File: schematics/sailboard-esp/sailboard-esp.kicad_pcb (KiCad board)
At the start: 2 copper layers, 91.4 x 51.4 mm, 40 parts, among them IC1 TXB0108PWR, U1 AP2112K-3.3, U2 L293D

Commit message: added changelog and tweaks.
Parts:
- removed the REF** at (228.6, 49.8)
- added C4: 470uF, Capacitor_THT:CP_Radial_D8.0mm_P3.50mm, F.Cu at (227.1, 50.4)
- moved RUDDER1 4.43 mm to (238.0, 56.9), turned to 90 degrees
- moved SOLARIN1 1.60 mm to (236.3, 62.8)
- moved BATCHRG 0.93 mm to (236.3, 69.8)
- renumbered BATCHRG1 to BATCHRG
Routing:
- net +5V: track 245.8 -> 264.5 mm
- net GND: track 353.1 -> 367.1 mm
- net /RUDDER_PWM_5V: track 43.3 -> 39.7 mm
- net /Power/Solar Pos: track 26.9 -> 28.5 mm
- net /Power/Battery Charge Pos: track 28.7 -> 29.6 mm
- net /Power/Battery Charge Neg: track 7.62 -> 6.96 mm
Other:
- board text added: "SailBOARD 1.3 (12/9/22) by rmcl"
- board text removed: "SailBOARD 1.2 (12/9/22) by rmcl"

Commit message: v1.3.
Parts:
- added R6: 47K ARRAY, YC164-JR-0747KL:RESCAXE80P320X160X70-8N, F.Cu at (177.9, 66.5)
- added R7: 47K ARRAY, YC164-JR-0747KL:RESCAXE80P320X160X70-8N, F.Cu at (156.2, 65.0)
- moved ArduCam1 17.4 mm to (163.4, 25.0), turned to 0 degrees
- moved C2 1.23 mm to (171.4, 30.9)
- moved C1 0.28 mm to (209.6, 39.4)
- renumbered BATCHRG to BATCHRG1
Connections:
- COMPASS1 pad 1: GND -> +3.3V
- COMPASS1 pad 2: +3.3V -> GND
- ESP32 pad 11: unconnected-(ESP32-Pad11) -> /Microcontroller/PROP_PWM
- ESP32 pad 25: Net-(ESP32-Pad25) -> unconnected-(ESP32-Pad25)
- IC1 pad 4: Net-(ESP32-Pad25) -> /Microcontroller/PROP_PWM
- IRIDIUM1 pad 1: /IRIDIUM_RX -> GND
- IRIDIUM1 pad 10: GND -> /IRIDIUM_RX
- IRIDIUM1 pad 3: unconnected-(IRIDIUM1-Pad3) -> +5V
- IRIDIUM1 pad 4: unconnected-(IRIDIUM1-Pad4) -> /IRIDIUM_SLEEP
- IRIDIUM1 pad 5: /IRIDIUM_RING -> /IRIDIUM_TX
- IRIDIUM1 pad 6: /IRIDIUM_TX -> /IRIDIUM_RING
- IRIDIUM1 pad 7: /IRIDIUM_SLEEP -> unconnected-(IRIDIUM1-Pad7)
- IRIDIUM1 pad 8: +5V -> unconnected-(IRIDIUM1-Pad8)
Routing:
- net +3.3V: track 255.0 -> 274.8 mm, vias 2 -> 7
- net /Microcontroller/PROP_PWM: track 0.00 -> 19.5 mm
- net Net-(ESP32-Pad25): track 18.4 -> 0.00 mm
- net /ARDUCAM_CS: track 66.8 -> 84.8 mm
- net /MOSI: track 22.2 -> 39.1 mm
- net /SDCARD_SCK: track 44.1 -> 59.5 mm, vias 1 -> 3
- net GND: track 367.1 -> 378.7 mm, vias 3 -> 4
- net /SDCARD_D0: track 66.1 -> 76.5 mm, vias 1 -> 3
- net /SCL: track 113.2 -> 103.4 mm, vias 2 -> 1
- net /SDCARD_D1: track 61.7 -> 70.3 mm
- net /SCK: track 39.7 -> 47.6 mm
- net /IRIDIUM_RX: track 69.8 -> 77.3 mm
- net /IRIDIUM_SLEEP: track 48.2 -> 41.5 mm
- net /SDA: track 130.3 -> 137.0 mm
- net /SDCARD_CMD: track 61.9 -> 68.4 mm
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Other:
- board text added: "SailBOARD 1.3 (12/22/22) by rmcl"
- board text removed: "SailBOARD 1.3 (12/9/22) by rmcl"

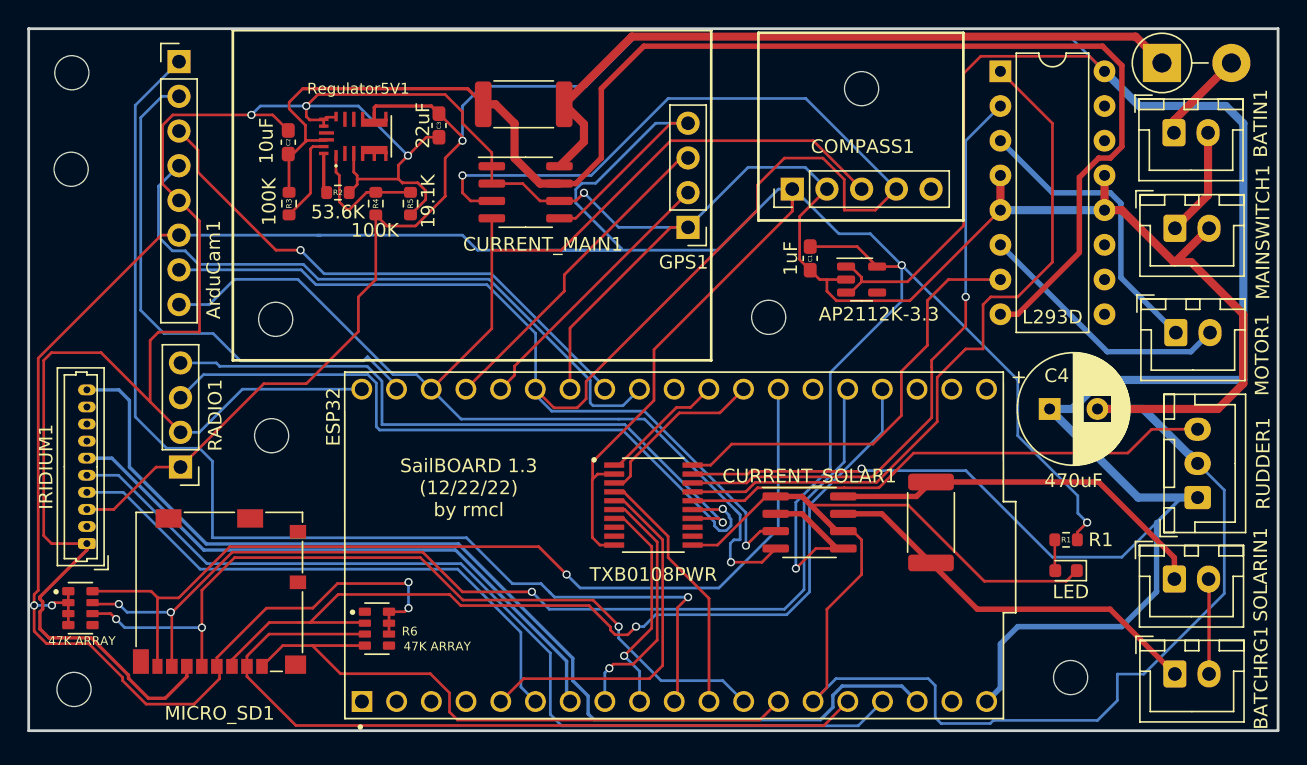
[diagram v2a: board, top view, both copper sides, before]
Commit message: rearrange pins to avoid ESP32 reserved / wonky pins.
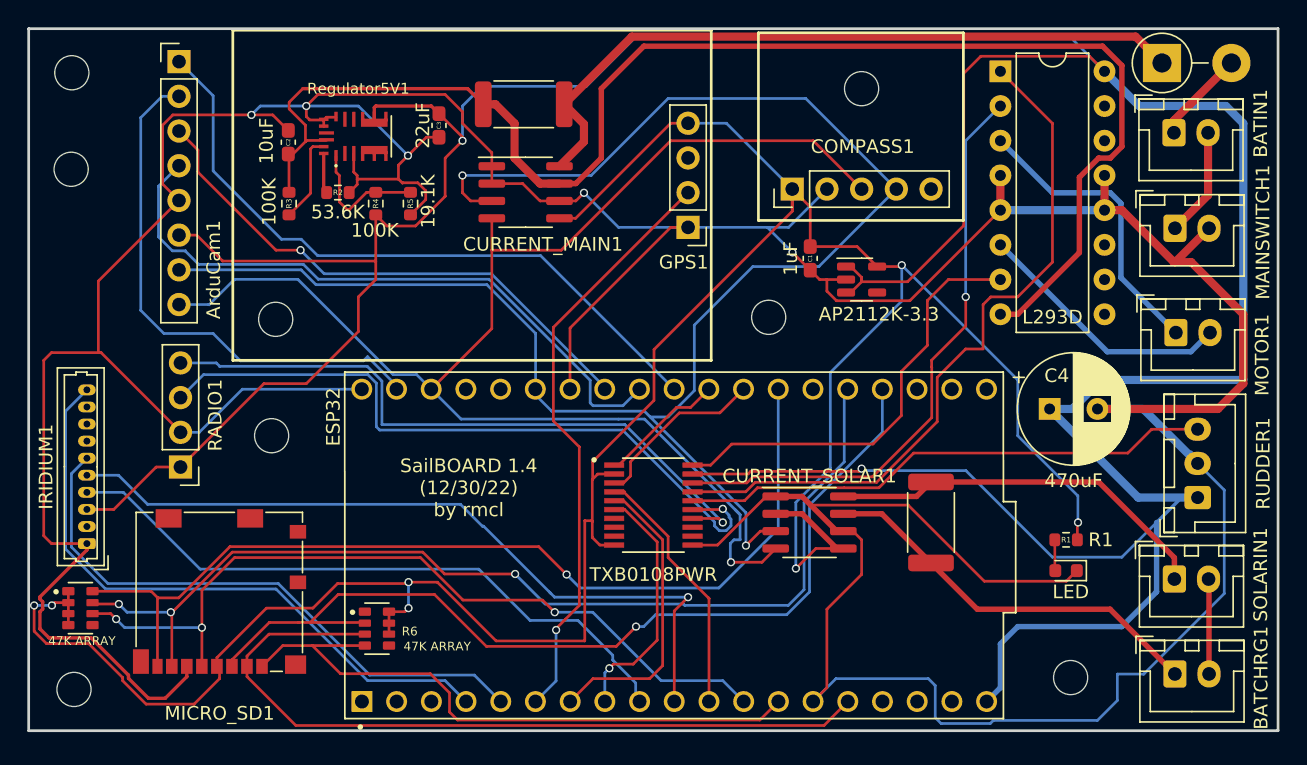
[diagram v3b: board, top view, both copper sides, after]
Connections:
- ArduCam1 pad 6: +3.3V -> +5V
- ESP32 pad 10: /ARDUCAM_CS -> /IRIDIUM_TX
- ESP32 pad 16: /IRIDIUM_TX -> unconnected-(ESP32-Pad16)
- ESP32 pad 17: /IRIDIUM_RX -> unconnected-(ESP32-Pad17)
- ESP32 pad 29: unconnected-(ESP32-Pad29) -> /ARDUCAM_CS
- ESP32 pad 34: /GPS_TX -> unconnected-(ESP32-Pad34)
- ESP32 pad 35: /GPS_RX -> unconnected-(ESP32-Pad35)
- ESP32 pad 4: unconnected-(ESP32-Pad4) -> /IRIDIUM_RX
- ESP32 pad 5: /Microcontroller/RUDDER_PWM -> /IRIDIUM_RING
- ESP32 pad 6: /IRIDIUM_SLEEP -> /GPS_TX
- ESP32 pad 7: /IRIDIUM_RING -> /Microcontroller/RUDDER_PWM
- ESP32 pad 9: /Microcontroller/RADIO_CHAN2 -> /IRIDIUM_SLEEP
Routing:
- net +3.3V: track 274.8 -> 202.3 mm
- net /ARDUCAM_CS: track 84.8 -> 49.4 mm, vias 1 -> 0
- net /IRIDIUM_RX: track 77.3 -> 46.2 mm
- net /GPS_RX: track 24.0 -> 0.00 mm
- net /GPS_TX: track 20.1 -> 43.4 mm, vias 0 -> 1
- net /Microcontroller/RADIO_CHAN2: track 16.2 -> 0.00 mm, vias 1 -> 0
- net +5V: track 265.0 -> 280.2 mm
- net /IRIDIUM_TX: track 69.2 -> 55.9 mm, vias 0 -> 1
- net /SDA: track 137.0 -> 124.8 mm
- net GND: track 378.7 -> 369.6 mm, vias 4 -> 5
- net /IRIDIUM_SLEEP: track 41.5 -> 47.8 mm
- net /Microcontroller/RUDDER_PWM: track 26.9 -> 21.8 mm
- net /IRIDIUM_RING: track 44.3 -> 43.1 mm
- net /SDCARD_CMD: track 68.4 -> 69.0 mm
- net /SDCARD_SCK: track 59.5 -> 59.0 mm
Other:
- board text added: "SailBOARD 1.4 (12/30/22) by rmcl"
- board text removed: "SailBOARD 1.3 (12/22/22) by rmcl"
